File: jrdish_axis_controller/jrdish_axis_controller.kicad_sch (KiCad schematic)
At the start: 0 parts

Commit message: Building first version...
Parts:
- added C1: 4.7uF, PCM_JLCPCB:C_0402, symbol PCM_JLCPCB-Capacitors:0402,4.7uF
- added C10, C9: 6.8pF, PCM_JLCPCB:C_0402, symbol PCM_JLCPCB-Capacitors:0402,6.8pF
- added C11, C2, C3, C4, C5, C8: 100nF, PCM_JLCPCB:C_0402, symbol PCM_JLCPCB-Capacitors:0402,100nF
- added C6: 10nF, PCM_JLCPCB:C_0402, symbol PCM_JLCPCB-Capacitors:0402,10nF
- added C7, C9: 1uF, PCM_JLCPCB:C_0402, symbol PCM_JLCPCB-Capacitors:0402,1uF
- added R1, R25: 10kΩ, PCM_JLCPCB:R_0402, symbol PCM_JLCPCB-Resistors:0402,10kΩ
- added U1: STM32G474CBT6, MyParts:LQFP-48_L7.0-W7.0-P0.50-LS9.0-BL, symbol MyParts:STM32G474CBT6
- added X1: NX2016SA-16MHZ-EXS00A-CS07826, MyParts:CRYSTAL-SMD_4P-L2.0-W1.6-BL, symbol MyParts:NX2016SA-16MHZ-EXS00A-CS07826
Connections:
- new net: R25.1, U1.45 (PB8-BOOT0)
- new net 3.3V_MCU: C1.1, C2.1, C3.1, C4.1, C5.1, C6.1, C7.1, C8.1, C9.1, R1.1, U1.1 (VBAT), U1.20 (VREF+), U1.21 (VDDA), U1.24 (VDD), U1.36 (VDD), U1.48 (VDD)
- new net GND_MCU: C1.2, C10.2, C11.2, C2.2, C3.2, C4.2, C5.2, C6.2, C7.2, C8.2, C9.1, C9.2, R25.2, U1.19 (VSSA), U1.23 (VSS), U1.35 (VSS), U1.47 (VSS), X1.2 (GND), X1.4 (GND)
- new net NRST: C11.1, R1.2, U1.7 (PG10-NRST)
- new net OSC_IN: C9.2, U1.5 (PF0-OSC_IN), X1.1
- new net OSC_OUT: C10.1, U1.6 (PF1-OSC_OUT), X1.3
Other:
- added sheet Axis Control (axis_control.kicad_sch)
- added sheet I2C (i2c.kicad_sch)
- added sheet Power (power.kicad_sch)
- added sheet RS485 (RS485.kicad_sch)
- note added: "16MHz XTAL"
- note added: "4.7uF Cap centrally located"
- note added: "Place 100nF caps close to their respective pins"
- note added: "Power Flags"
- note added: "VDDA Caps"
- note added: "VREF+ Caps"

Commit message: Updates
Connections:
- net 3.3V_MCU renamed 3.3V
- net GND_MCU renamed GND
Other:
- moved on the sheet: C10, C9, X1

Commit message: Passes ERC
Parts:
- removed U1: STM32G474CBT6, MyParts:LQFP-48_L7.0-W7.0-P0.50-LS9.0-BL, symbol MyParts:STM32G474CBT6
- added J1: Conn_ARM_SWD_TagConnect_TC2030-NL, Connector:Tag-Connect_TC2030-IDC-NL_2x03_P1.27mm_Vertical, symbol Connector:Conn_ARM_SWD_TagConnect_TC2030-NL
- added LED1: LTST-S270KGKT, MyParts:LED-SMD_L1.7-W0.6-RD, symbol MyParts:LTST-S270KGKT
- added R3: 330Ω, PCM_JLCPCB:R_0402, symbol PCM_JLCPCB-Resistors:0402,330Ω
- added SW1: DSHP04TSGER, MyParts:SW-SMD_8P-L6.7-W5.4-P1.27-LS8.4, symbol MyParts:DSHP04TSGER
- added U1: STM32G474CET6, MyParts:LQFP-48_L7.0-W7.0-P0.50-LS9.0-BL, symbol MyParts:STM32G474CET6
- renumbered C11 to C10, C10 to C11, C9 to C12, R25 to R1, R1 to R2
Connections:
- net 3.3V: now also J1.1 (VCC), U1.1 (VBAT), U1.20 (VREF+), U1.21 (VDDA), U1.24 (VDD), U1.36 (VDD), U1.48 (VDD)
- net GND: now also J1.5 (GND), LED1.1 (K), SW1.5 (B4), SW1.6 (B3), SW1.7 (B2), SW1.8 (B1), U1.19 (VSSA), U1.23 (VSS), U1.35 (VSS), U1.47 (VSS)
- net NRST: now also J1.3 (~{RESET}), U1.7 (PG10-NRST)
- net OSC_IN: now also U1.5 (PF0-OSC_IN)
- net OSC_OUT: now also U1.6 (PF1-OSC_OUT)
- net at R1.1: now also U1.45 (PB8-BOOT0)
- new net: SW1.4 (A4), U1.29 (PB15)
- new net: SW1.3 (A3), U1.31 (PA9)
- new net: SW1.2 (A2), U1.32 (PA10)
- new net: SW1.1 (A1), U1.33 (PA11)
- new net: R3.1, U1.34 (PA12)
- new net: LED1.2 (A), R3.2
- new net DIR_MCU: U1.17 (PB1)
- new net ENC_A_MCU: U1.8 (PA0)
- new net ENC_B_MCU: U1.9 (PA1)
- new net ENC_Z_MCU: U1.10 (PA2)
- new net FAN_MCU: U1.11 (PA3)
- new net LIMIT_SW1_MCU: U1.12 (PA4)
- new net LIMIT_SW2_MCU: U1.13 (PA5)
- new net MF_MCU: U1.18 (PB2)
- new net PUL_MCU: U1.16 (PB0)
- new net SCL_MCU: U1.30 (PA8)
- new net SDA_MCU: U1.42 (PB5)
- new net SWCLK: J1.4 (SWCLK), U1.38 (PA14)
- new net SWDIO: J1.2 (SWDIO), U1.37 (PA13)
- new net SWO: J1.6 (SWO), U1.40 (PB3)
- new net USART1_RX_MCU: U1.44 (PB7)
- new net USART1_TX_MCU: U1.43 (PB6)
- no-connect marks 0 -> 13
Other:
- sheet I2C renamed I2C and EEPROM
- added sheet Fan (fan.kicad_sch)
- added sheet Notes (notes.kicad_sch)
- note added: "2-Wire Connector"
- moved on the sheet: C10, R2

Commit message: PCB layout in progress
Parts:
- removed C1: 4.7uF, PCM_JLCPCB:C_0402, symbol PCM_JLCPCB-Capacitors:0402,4.7uF
- removed J1: Conn_ARM_SWD_TagConnect_TC2030-NL, Connector:Tag-Connect_TC2030-IDC-NL_2x03_P1.27mm_Vertical, symbol Connector:Conn_ARM_SWD_TagConnect_TC2030-NL
- removed R2: 10kΩ, PCM_JLCPCB:R_0402, symbol PCM_JLCPCB-Resistors:0402,10kΩ
- added C1: 4.7uF, PCM_JLCPCB:C_0603, symbol PCM_JLCPCB-Capacitors:0603,4.7uF
- added C13: 100nF, PCM_JLCPCB:C_0402, symbol PCM_JLCPCB-Capacitors:0402,100nF
- added H1: 210S-1*2P L=11.6MMGold-plated black, MyParts:HDR-TH_2P-P2.54-V-M-1, symbol MyParts:210S-1*2PL=11.6MMGold-platedblack
- added J1: Conn_ARM_SWD_TagConnect_TC2030, Connector:Tag-Connect_TC2030-IDC-FP_2x03_P1.27mm_Vertical, symbol Connector:Conn_ARM_SWD_TagConnect_TC2030
- added R1: 1kΩ, PCM_JLCPCB:R_0402, symbol PCM_JLCPCB-Resistors:0402,1kΩ
- renumbered R1 to R2
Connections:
- net 3.3V: now also C1.1, C13.1, J1.1 (VCC), R1.1
- net GND: now also R2.1, C1.2, C13.2, J1.5 (GND); no longer R2.2
- net NRST: now also J1.3 (~{RESET})
- net SWCLK: now also J1.4 (SWCLK)
- net SWDIO: now also J1.2 (SWDIO)
- net SWO: now also J1.6 (SWO)
- net at U1.45 (PB8-BOOT0): now also R2.2, H1.2; no longer R2.1
- new net: H1.1, R1.2
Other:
- note added: "One Axis Controller"
- note added: "Place jumper for force into bootloader mode"
- note added: "Purpose: Control one Axis of a motor controlled system. - Modbus commands over isolated RS485. - MCU outputs motor PWM, direction, enable/disable - Input from encoder connected to motor output - Host provides configuration and position commands - MCU runs a PID loop to position/move motor - Onboard temperature sensor, MCU can turn fan on/off - I2C extender for sensors placed at the axis"
- note added: "Switch: Pins 1,2,3 are the address of this board on the RS485 bus. Pin 4 is an extra pin that may be of future use, but not used now."
- note added: "The one with 4 holes for the clip"
- company: (none) -> JRSeti
- title: (none) -> MCU/Overview
- moved on the sheet: C10, C11, C12, R2, X1

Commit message: Layout no ERC errors
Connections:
- net RS485_DE_MCU: now reaches U1.46 (PB9)
- no-connect marks 13 -> 12
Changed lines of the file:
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@@
-	)
-	(no_connect
-		(at 104.14 46.99)
 	)
 	(no_connect
@@
 		(pts
 			(xy 46.99 153.67) (xy 46.99 154.94)
+		)
+		(stroke
+			(width 0)
+			(type default)
+		)
+	)
+	(wire
+		(pts
+			(xy 104.14 46.99) (xy 105.41 46.99)
 		)
 		(stroke
@@
 				(hide yes)
 			)
+		)
+	)
+	(global_label "RS485_DE_MCU"
+		(shape input)
+		(at 105.41 46.99 0)
+		(fields_autoplaced yes)
+		(effects
+			(font
+				(size 1.27 1.27)
+			)
+			(justify left)
+		)
+		(property "Intersheetrefs" "${INTERSHEET_REFS}"
+			(at 122.9093 46.99 0)
+			(effects
+				(font
+					(size 1.27 1.27)
+				)
+				(justify left)
+				(hide yes)
+			)

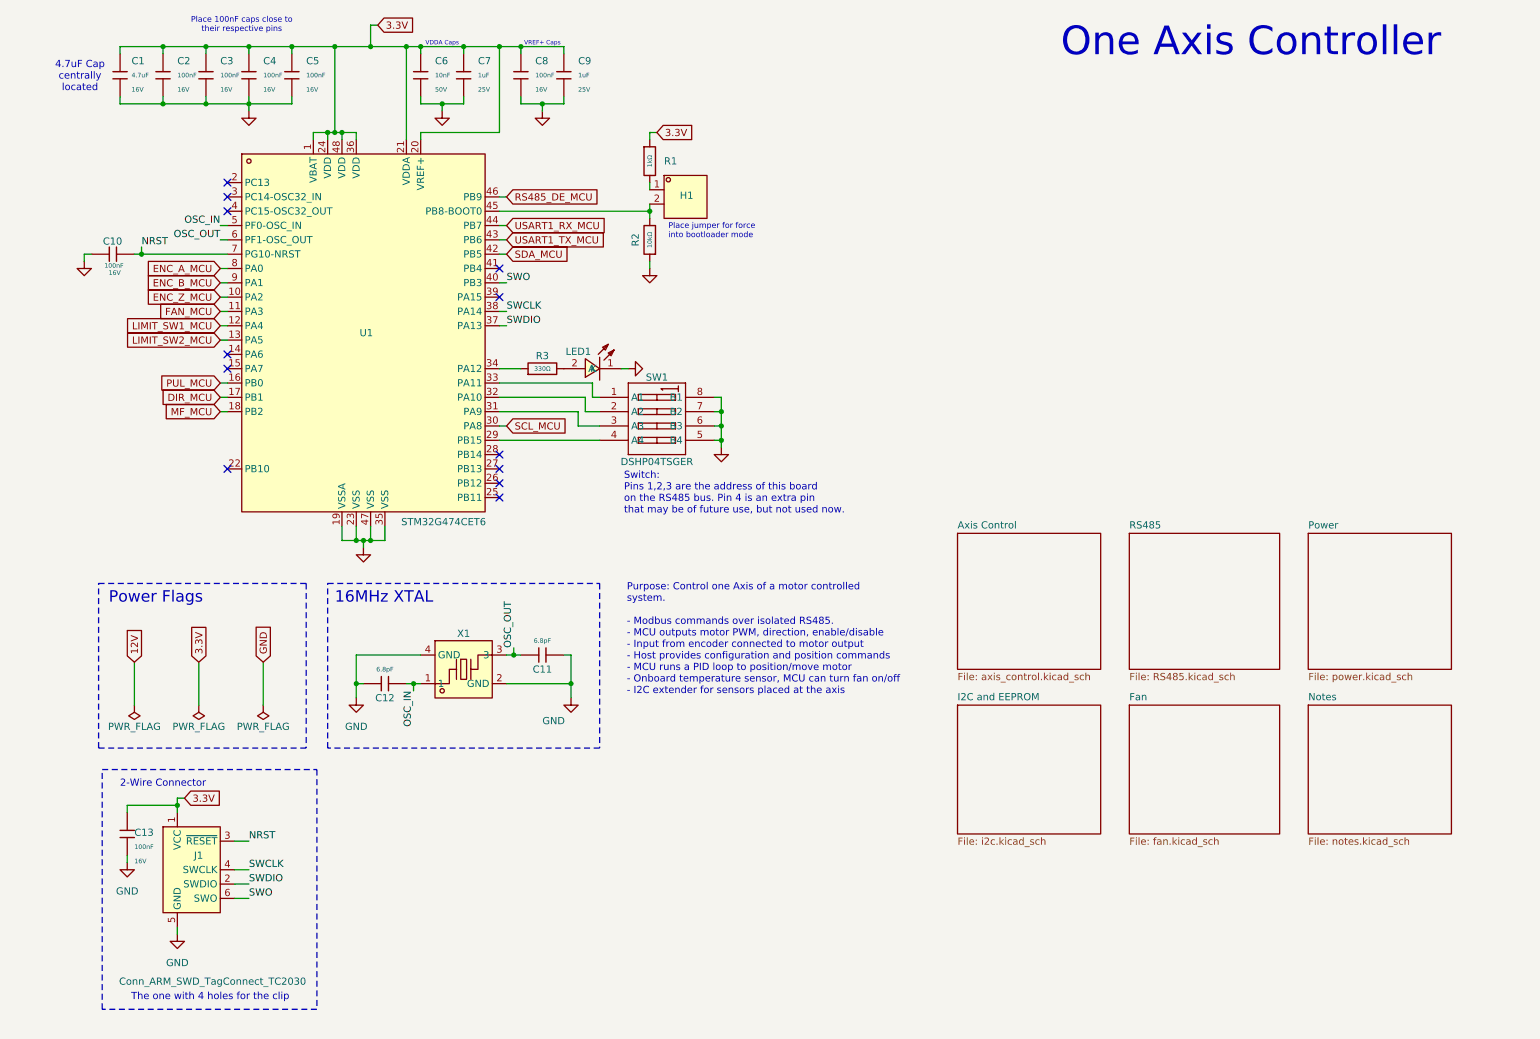
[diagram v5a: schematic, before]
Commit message: New 64pin version - 2 axes
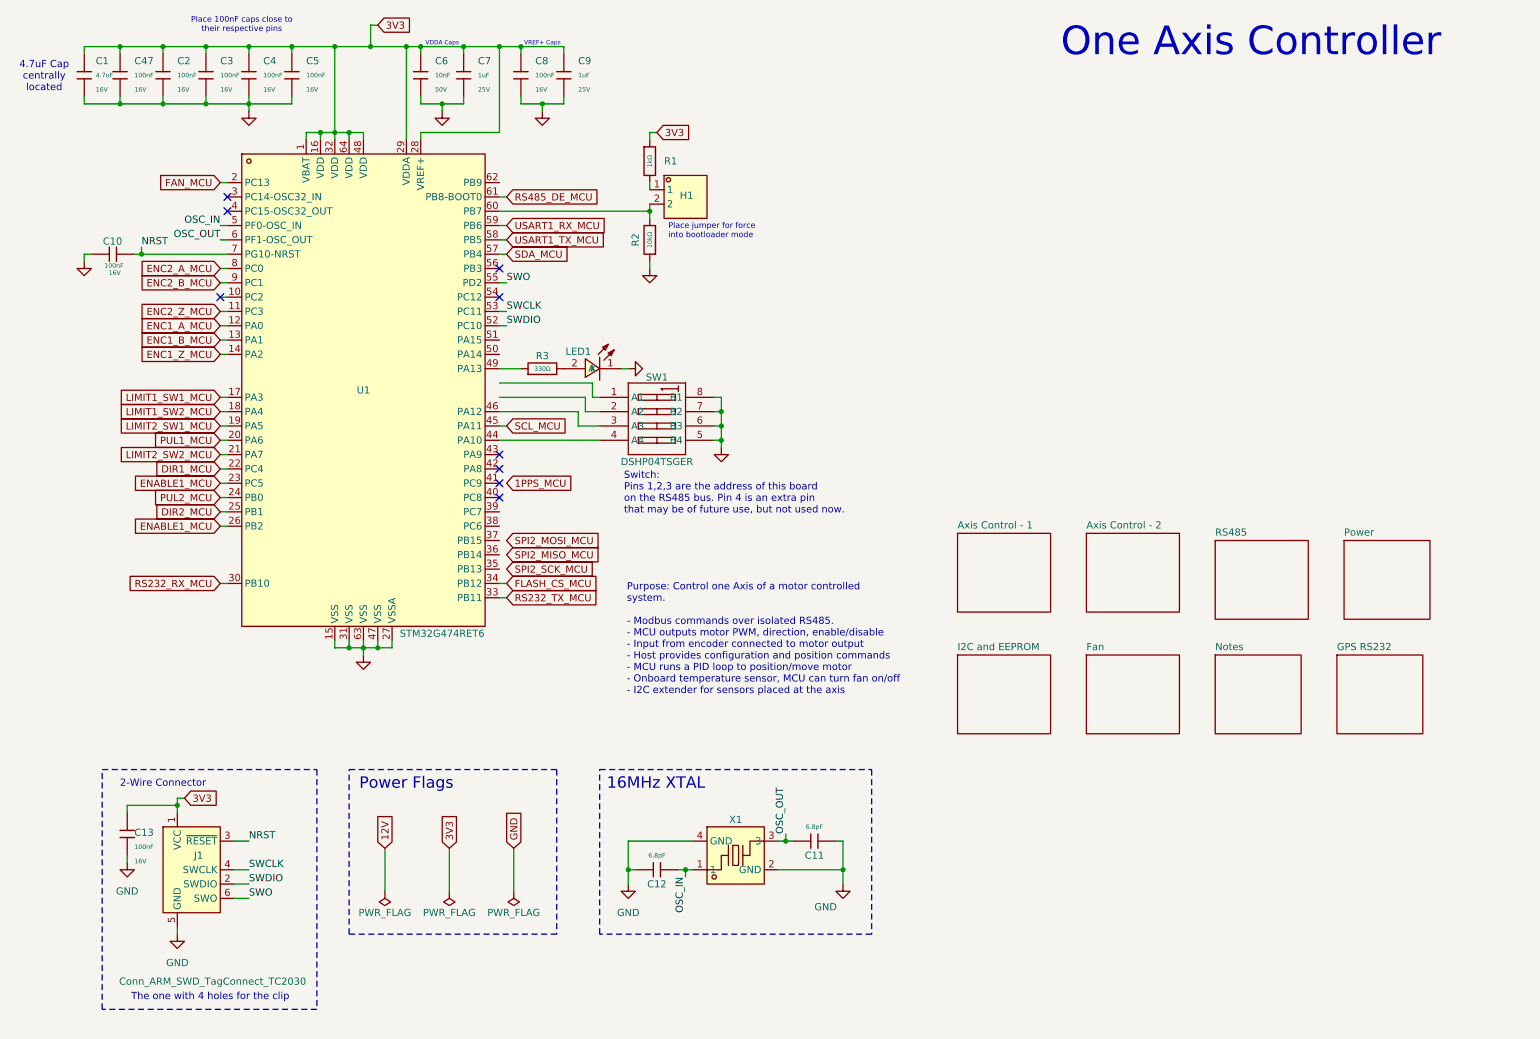
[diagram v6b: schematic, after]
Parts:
- removed U1: STM32G474CET6, MyParts:LQFP-48_L7.0-W7.0-P0.50-LS9.0-BL, symbol MyParts:STM32G474CET6
- added C47: 100nF, PCM_JLCPCB:C_0402, symbol PCM_JLCPCB-Capacitors:0402,100nF
- added U1: STM32G474RET6, MyParts:LQFP-64_L10.0-W10.0-P0.50-LS12.0-BL, symbol MyParts:STM32G474RET6
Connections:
- net FAN_MCU: now also U1.2 (PC13)
- net GND: now also C47.2, U1.15 (VSS), U1.27 (VSSA), U1.31 (VSS), U1.47 (VSS), U1.63 (VSS)
- net NRST: now also U1.7 (PG10-NRST)
- net OSC_IN: now also U1.5 (PF0-OSC_IN)
- net OSC_OUT: now also U1.6 (PF1-OSC_OUT)
- net RS485_DE_MCU: now also U1.61 (PB8-BOOT0)
- net SCL_MCU: now also U1.45 (PA11)
- net SDA_MCU: now also U1.57 (PB4)
- net SWCLK: now also U1.53 (PC11)
- net SWDIO: now also U1.52 (PC10)
- net SWO: now also U1.55 (PD2)
- net USART1_RX_MCU: now also U1.59 (PB6)
- net USART1_TX_MCU: now also U1.58 (PB5)
- net at H1.2, R2.2: now also U1.60 (PB7)
- net at SW1.4 (A4): now also U1.44 (PA10)
- net at SW1.3 (A3): now also U1.46 (PA12)
- net at R3.1: now also U1.49 (PA13)
- net 3.3V renamed 3V3
- net 3V3: now also C47.1, U1.1 (VBAT), U1.16 (VDD), U1.28 (VREF+), U1.29 (VDDA), U1.32 (VDD), U1.48 (VDD), U1.64 (VDD)
- new net DIR1_MCU: U1.22 (PC4)
- new net DIR2_MCU: U1.25 (PB1)
- new net ENABLE1_MCU: U1.23 (PC5), U1.26 (PB2)
- new net ENC1_A_MCU: U1.12 (PA0)
- new net ENC1_B_MCU: U1.13 (PA1)
- new net ENC1_Z_MCU: U1.14 (PA2)
- new net ENC2_A_MCU: U1.8 (PC0)
- new net ENC2_B_MCU: U1.9 (PC1)
- new net ENC2_Z_MCU: U1.11 (PC3)
- new net FLASH_CS_MCU: U1.34 (PB12)
- new net LIMIT1_SW1_MCU: U1.17 (PA3)
- new net LIMIT1_SW2_MCU: U1.18 (PA4)
- new net LIMIT2_SW1_MCU: U1.19 (PA5)
- new net LIMIT2_SW2_MCU: U1.21 (PA7)
- new net PUL1_MCU: U1.20 (PA6)
- new net PUL2_MCU: U1.24 (PB0)
- new net RS232_RX_MCU: U1.30 (PB10)
- new net RS232_TX_MCU: U1.33 (PB11)
- no-connect marks 12 -> 9
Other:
- sheet Axis Control renamed Axis Control - 1
- added sheet Axis Control - 2 (axis_control_2.kicad_sch)
- added sheet GPS RS232 (gps_rs232.kicad_sch)
- sheet Axis Control - 1: file axis_control.kicad_sch -> axis_control_1.kicad_sch
- moved on the sheet: C1, C11, C12, X1

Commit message: Continuing layout
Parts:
- renumbered C9 to C10, C10 to C11, C13 to C12, C11 to C13, C12 to C14, C47 to C2, C2 to C3, C3 to C4, C4 to C5, C5 to C6, C6 to C7, C7 to C8, C8 to C9
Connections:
- net RS485_DE_MCU is gone; now on an unnamed net: U1.61 (PB8-BOOT0)
- net 1PPS_MCU: now also U1.62 (PB9)
- net ENABLE1_MCU: no longer U1.26 (PB2)
- net SCL_MCU: now also U1.38 (PC6); no longer U1.45 (PA11)
- net SDA_MCU: now also U1.39 (PC7); no longer U1.57 (PB4)
- net SPI2_MISO_MCU: now also U1.36 (PB14)
- net SPI2_MOSI_MCU: now also U1.37 (PB15)
- net SPI2_SCK_MCU: now also U1.35 (PB13)
- net SWCLK: now also U1.50 (PA14); no longer U1.53 (PC11)
- net SWDIO: now also U1.49 (PA13); no longer U1.52 (PC10)
- net SWO: now also U1.56 (PB3); no longer U1.55 (PD2)
- net at H1.2, R2.2: no longer U1.60 (PB7)
- net at R3.1: now also U1.46 (PA12); no longer U1.49 (PA13)
- net CONFIG_SW: now reaches U1.42 (PA8)
- net CONFIG_SW: now also SW1.4 (A4)
- net ADDR2: now reaches U1.43 (PA9)
- net ADDR2: now also SW1.3 (A3)
- net ADDR1: now reaches U1.44 (PA10)
- net ADDR1: now also SW1.2 (A2); no longer SW1.4 (A4)
- net ADDR0: now reaches SW1.1 (A1)
- net ADDR0: now also U1.45 (PA11)
- net USART1_RX_MCU renamed RS485_1_TX_MCU
- net USART1_TX_MCU renamed RS485_1_DE_MCU
- new net ENABLE2_MCU: U1.26 (PB2)
- new net RS485_1_RX_MCU: U1.60 (PB7)
- new net RS485_2_DE_MCU: U1.55 (PD2)
- new net RS485_2_RX_MCU: U1.53 (PC11)
- new net RS485_2_TX_MCU: U1.52 (PC10)
- no-connect marks 9 -> 8
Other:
- note added: "Dual Axis Controller"
- note added: "Purpose: Control 2 Axes of a motor controlled system. - Modbus commands over isolated RS485. - MCU outputs motor PWM, direction, enable/disable - Input from encoder connected to motor output - Host provides configuration and position commands - MCU runs a PID loop to position/move motor - Onboard temperature sensor, MCU can turn fan on/off - I2C extender for sensors placed at the axis"
- note added: "Switch: Pins 1,2,3 are the address of this board on the RS485_1 bus. Pin 4 is an extra pin that may be of future use, but not used now."
- note removed: "One Axis Controller"
- note removed: "Purpose: Control one Axis of a motor controlled system. - Modbus commands over isolated RS485. - MCU outputs motor PWM, direction, enable/disable - Input from encoder connected to motor output - Host provides configuration and position commands - MCU runs a PID loop to position/move motor - Onboard temperature sensor, MCU can turn fan on/off - I2C extender for sensors placed at the axis"
- note removed: "Switch: Pins 1,2,3 are the address of this board on the RS485 bus. Pin 4 is an extra pin that may be of future use, but not used now."
- moved on the sheet: H1, LED1, R1, R2, R3, SW1
